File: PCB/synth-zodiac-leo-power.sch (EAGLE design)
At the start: 54 parts

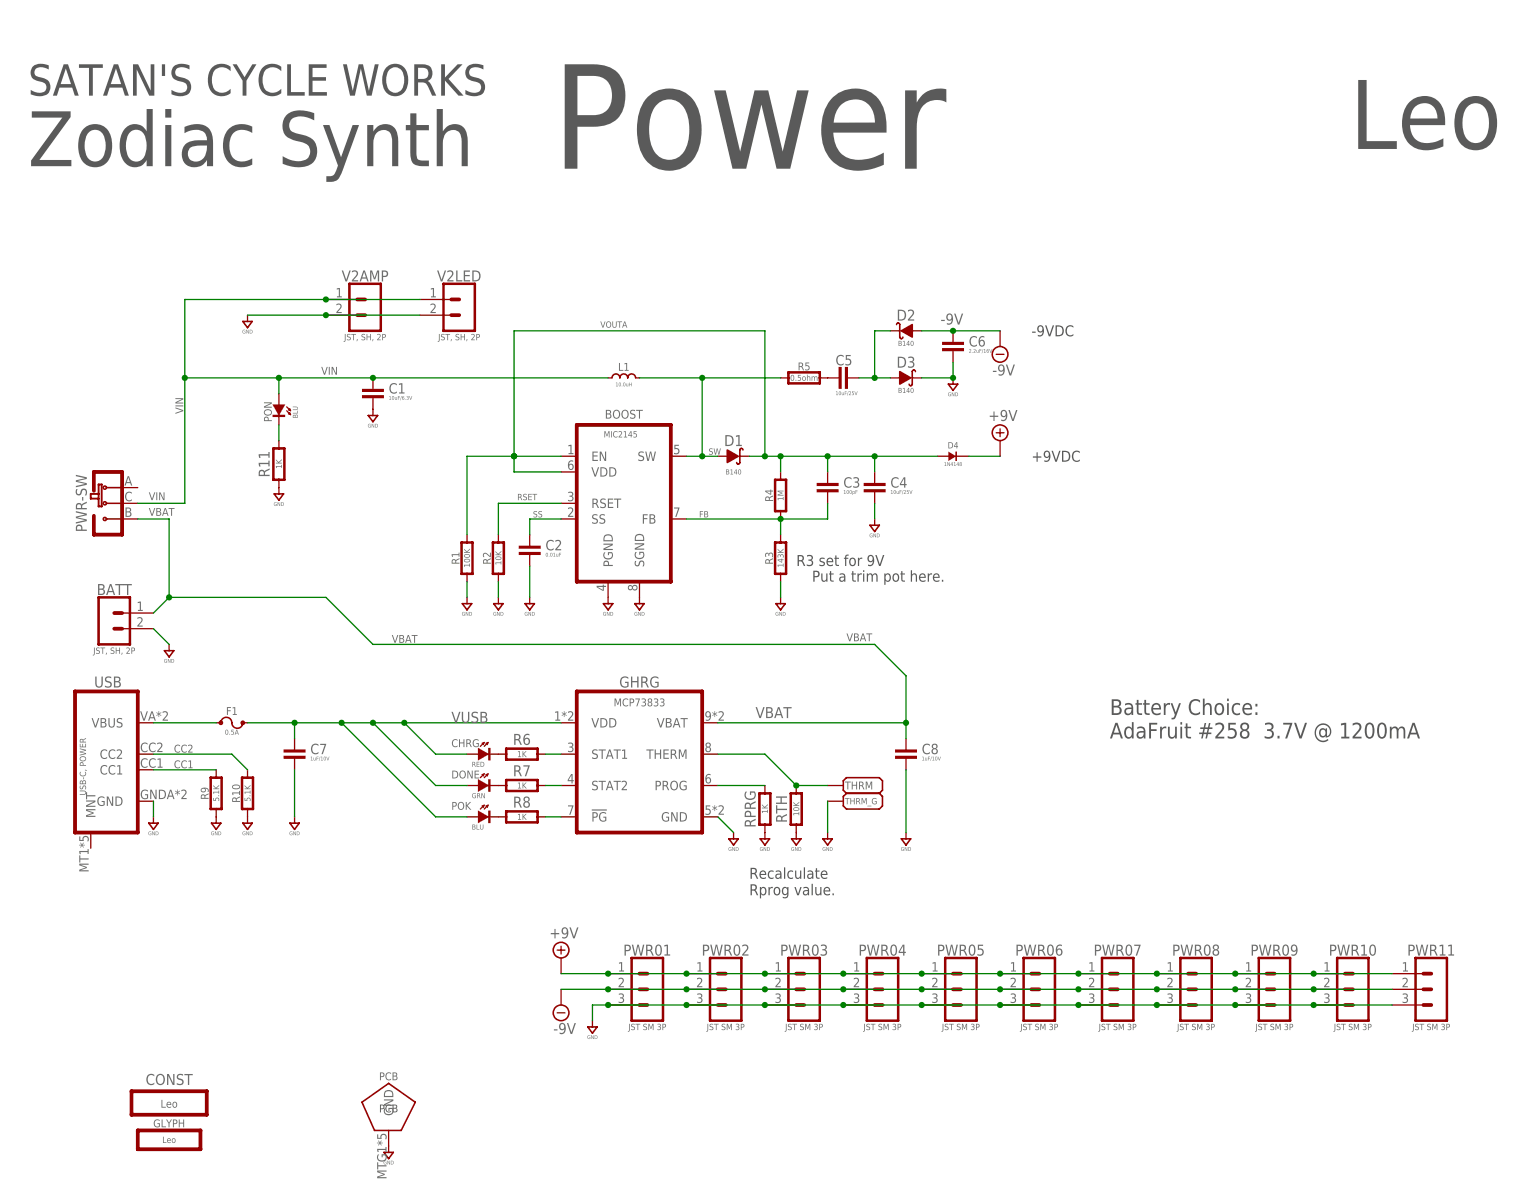
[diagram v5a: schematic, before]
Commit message: Update component value for charging rate.
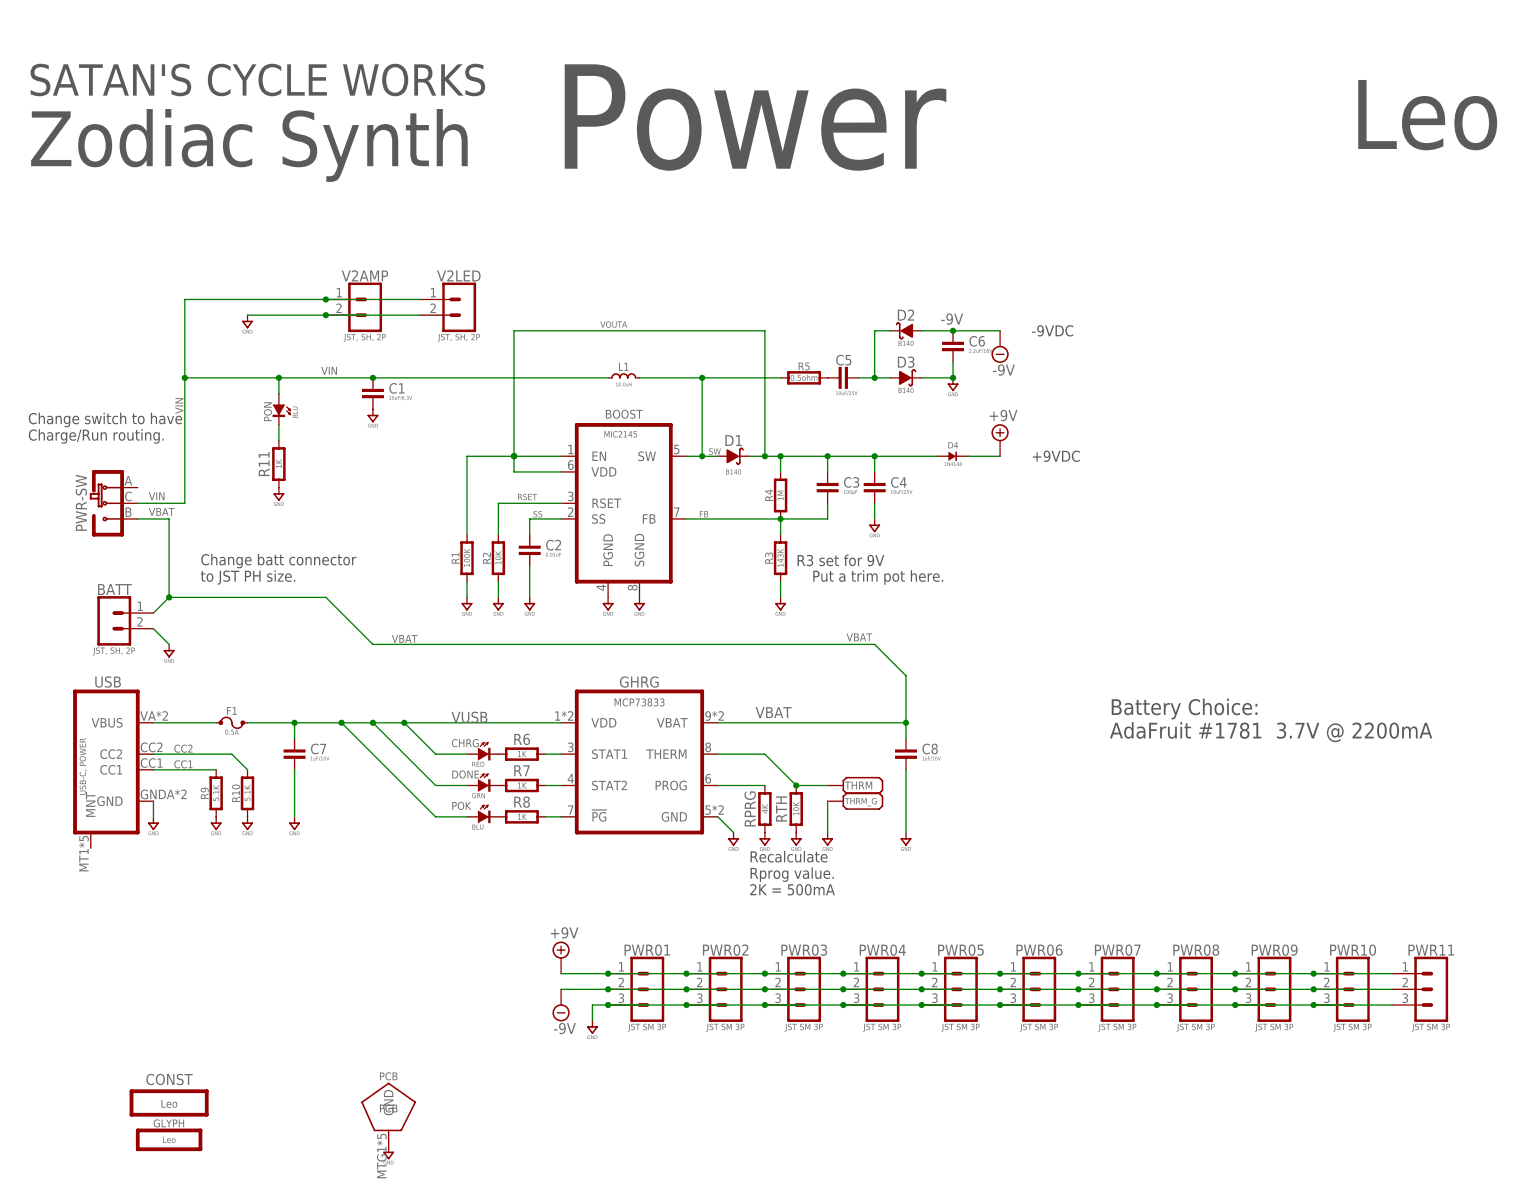
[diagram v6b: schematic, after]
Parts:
- RPRG: value 1K -> 4K
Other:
- note added: "Battery Choice: AdaFruit #1781 3.7V @ 2200mA"
- note added: "Change batt connector to JST PH size."
- note added: "Change switch to have Charge/Run routing."
- note added: "Recalculate Rprog value. 2K = 500mA"
- note removed: "Battery Choice: AdaFruit #258 3.7V @ 1200mA"
- note removed: "Recalculate Rprog value."
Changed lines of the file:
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@@
 <part name="R8" library="rlc" library_urn="urn:adsk.eagle:library:4192893" deviceset="RESISTOR" device="0603" package3d_urn="urn:adsk.eagle:package:4193040/5" value="1K"/>
 <part name="C8" library="rlc" library_urn="urn:adsk.eagle:library:4192893" deviceset="CAPACITOR" device="0603" package3d_urn="urn:adsk.eagle:package:4193021/5" value="1uF/10V"/>
-<part name="RPRG" library="rlc" library_urn="urn:adsk.eagle:library:4192893" deviceset="RESISTOR" device="0603" package3d_urn="urn:adsk.eagle:package:4193040/5" value="1K"/>
+<part name="RPRG" library="rlc" library_urn="urn:adsk.eagle:library:4192893" deviceset="RESISTOR" device="0603" package3d_urn="urn:adsk.eagle:package:4193040/5" value="4K"/>
 <part name="RTH" library="rlc" library_urn="urn:adsk.eagle:library:4192893" deviceset="RESISTOR" device="0603" package3d_urn="urn:adsk.eagle:package:4193040/5" value="10K"/>
 <part name="THRM_G" library="con-testpoints" library_urn="urn:adsk.eagle:library:7289188" deviceset="PAD" device="SMD-050X050" package3d_urn="urn:adsk.eagle:package:36472491/1"/>
@@
 <plain>
 <text x="180.34" y="71.12" size="2.54" layer="97">Battery Choice:
-AdaFruit #258  3.7V @ 1200mA</text>
+AdaFruit #1781  3.7V @ 2200mA</text>
 <text x="129.54" y="99.06" size="1.778" layer="97">R3 set for 9V</text>
 <text x="167.64" y="137.16" size="1.778" layer="97" align="center-left">-9VDC</text>
@@
 <text x="132.08" y="96.52" size="1.778" layer="97">Put a trim pot here.</text>
 <text x="121.92" y="45.72" size="1.778" layer="97">Recalculate
-Rprog value.</text>
+Rprog value.
+2K = 500mA</text>
 <text x="121.92" y="180.34" size="16.9164" layer="97" ratio="15" align="top-center">Power</text>
 <text x="5.08" y="172.72" size="8.89" layer="97" ratio="15" align="top-left">Zodiac Synth</text>
 <text x="243.84" y="177.8" size="11.176" layer="97" align="top-right">Leo</text>
 <text x="5.08" y="175.26" size="5.08" layer="97">SATAN'S CYCLE WORKS</text>
+<text x="5.08" y="119.38" size="1.778" layer="97">Change switch to have
+Charge/Run routing.</text>
+<text x="33.02" y="96.52" size="1.778" layer="97">Change batt connector
+to JST PH size.</text>
 </plain>
 <instances>
